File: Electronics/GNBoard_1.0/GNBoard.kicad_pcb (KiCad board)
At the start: 2 copper layers, 77.9 x 54.5 mm, 47 parts, among them K1 IR1, K10 IR4, K11 CNY_1, K12 CNY_2, K13 CNY_3, K14 CNY_4, K15 CNY_5, K16 CNY_6, K2 IR2, K3 SERVO_1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

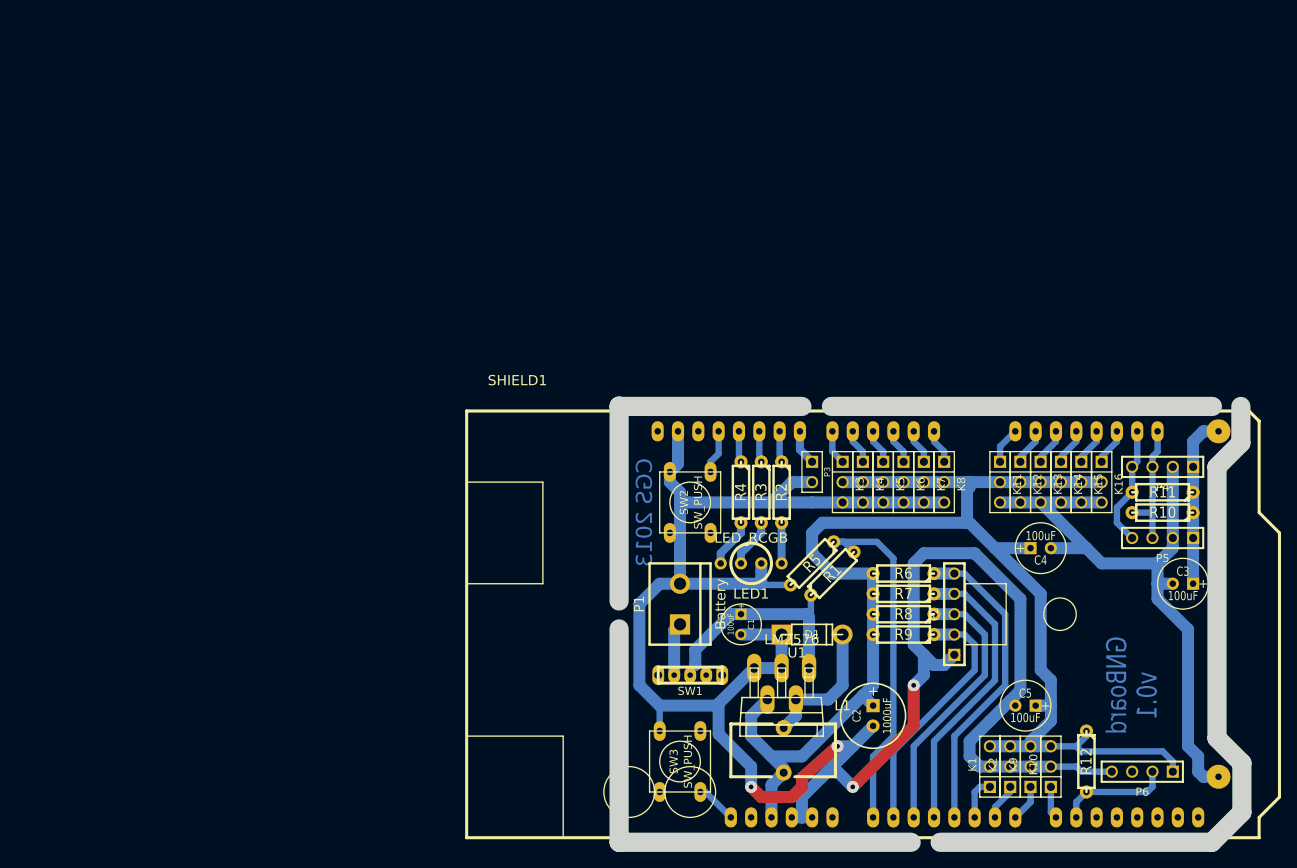
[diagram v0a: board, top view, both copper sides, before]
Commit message: Moved v0.1 to its own folder
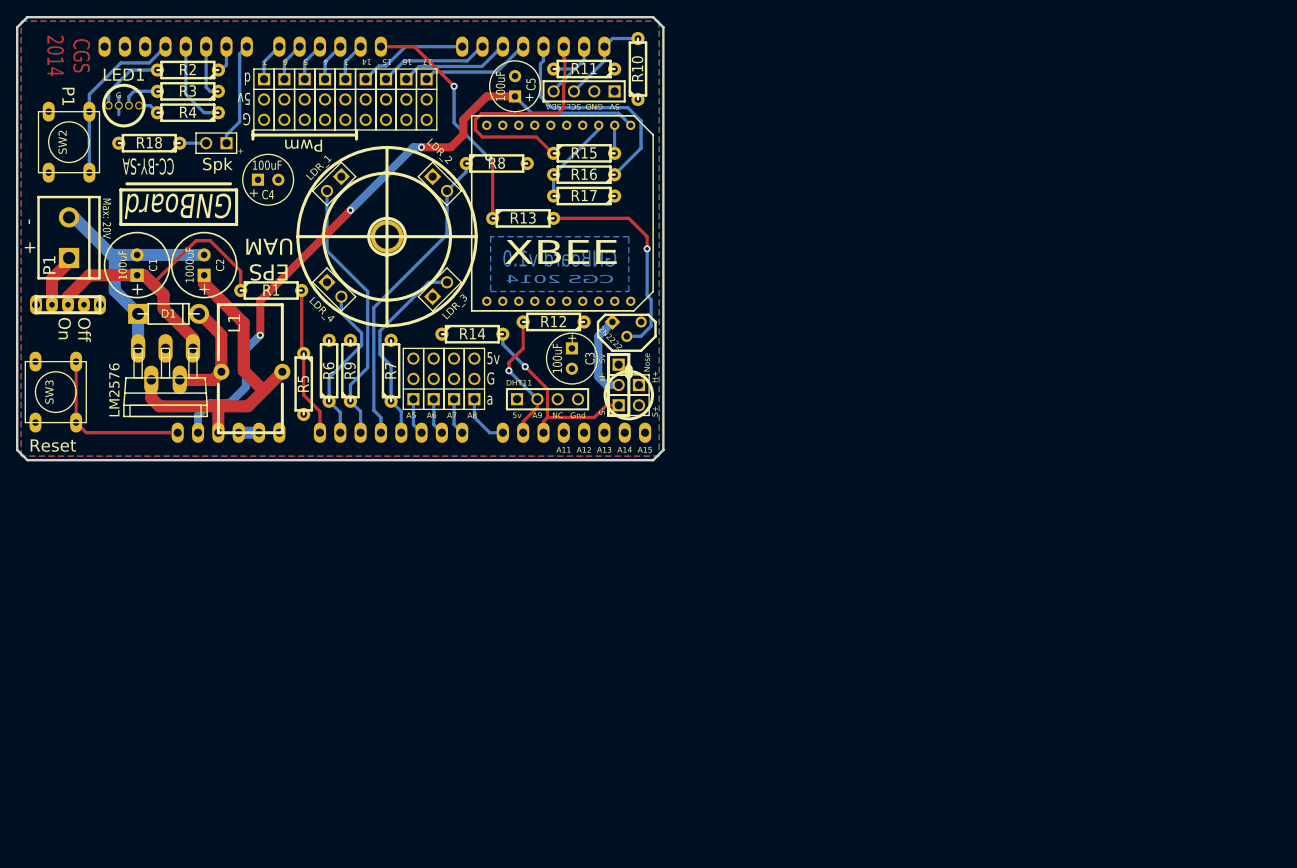
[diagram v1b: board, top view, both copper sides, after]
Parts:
- removed K15: CNY_5, PIN_ARRAY_3X1
- removed K16: CNY_6, PIN_ARRAY_3X1
- removed K8: SERVO_6, PIN_ARRAY_3X1
- added 1PIN: P***, ldr_drill, F.Cu at (96.7, 48.1)
- added M1: XBEE, xbee_r1-XBEE, F.Cu at (118.2, 45.1)
- added P10: Nose_Heater, PIN_ARRAY_2X1, F.Cu at (126.9, 66.6)
- added P11: CONN_1, PIN_ARRAY_1, F.Cu at (125.7, 64.1)
- added P7: LDR_3, PIN_ARRAY_2X1, F.Cu at (103.3, 54.7)
- added P8: LDR_4, PIN_ARRAY_2X1, F.Cu at (90.1, 54.7)
- added P9: Nose_Sense, PIN_ARRAY_2X1, F.Cu at (126.9, 69.1)
- added Q1: NPN, TO92-123, F.Cu at (126.7, 58.7)
- added R13: 10k, R3-LARGE_PADS, F.Cu at (113.7, 45.8)
- added R14: 10k, R3-LARGE_PADS, F.Cu at (107.4, 60.2)
- added R15: 4k7, R3-LARGE_PADS, F.Cu at (121.4, 37.6)
- added R16: 4k7, R3-LARGE_PADS, F.Cu at (121.4, 40.3)
- added R17: 7k5, R3-LARGE_PADS, F.Cu at (121.4, 43.0)
- added R18: 47, R3-LARGE_PADS, F.Cu at (67.0, 36.4)
- C1: footprint C1V5 -> C1V8
- L1: footprint Choke_Toroid_6,5x13mm_Vertical -> Choke_Toroid_8x16mm_Vertical
- LED1: footprint LED5_RGB_long_wide -> LED5_RGB_long
- P2: value CONN_5 -> LDR_1; footprint PIN_ARRAY_5x1 -> PIN_ARRAY_2X1
- P5: value I2C_2 -> LDR_2; footprint PIN_ARRAY_4x1 -> PIN_ARRAY_2X1
- R1: value 6k8 -> 62k
- R5: value 6k8 -> 20k
- SHIELD1: footprint ARDUINO_MEGA_SHIELD -> ARDUINO_MEGA_SHIELD_040pins_MOD
- SW1: footprint SWITCH_3Pin -> switch_power_custom
- moved C4 107.0 mm to (81.9, 40.9)
- moved C2 100.8 mm to (73.9, 51.6), turned to 90 degrees
- moved P5 100.6 mm to (103.3, 41.5), turned to 315 degrees
- moved C5 100.3 mm to (112.7, 29.3), turned to 90 degrees
- moved LED1 97.1 mm to (63.8, 31.7), turned to 0 degrees
- moved P2 94.4 mm to (90.1, 41.5), turned to 225 degrees
- moved K12 92.6 mm to (96.6, 30.9)
- moved K13 92.6 mm to (99.1, 30.9)
- moved K14 92.6 mm to (101.7, 30.9)
- moved K11 92.6 mm to (94.1, 30.9)
- moved R2 91.1 mm to (71.8, 27.2), turned to 180 degrees
- moved SW3 90.7 mm to (55.3, 67.5)
- moved SW1 90.5 mm to (56.8, 56.6)
- moved D1 89.9 mm to (69.4, 57.7)
- moved SW2 89.8 mm to (57.0, 36.2)
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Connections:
- C5 pad 1: +5V -> +3.3V
- P3 pad 2: GND -> N-0000014
- P5 pad 1: +5V -> GND
- P5 pad 2: GND -> LDR2
- P6 pad 3: N-0000082 -> (no net)
- SHIELD1 pad 13: N-0000067 -> (no net)
- SHIELD1 pad 18: CNY5 -> XB_DIN
- SHIELD1 pad 19: CNY6 -> XB_DOUT
- SHIELD1 pad 2: Servo6 -> Nose_heat
- SHIELD1 pad 3V3: N-0000040 -> +3.3V
- SHIELD1 pad AD1: LDR1 -> LDR4
- SHIELD1 pad AD10: N-0000041 -> Nose_Vout
- SHIELD1 pad AD11: N-0000039 -> (no net)
- SHIELD1 pad AD12: N-0000042 -> (no net)
- SHIELD1 pad AD13: N-0000043 -> (no net)
- SHIELD1 pad AD14: N-0000044 -> (no net)
- SHIELD1 pad AD15: N-0000045 -> (no net)
- SHIELD1 pad AD2: LDR2 -> LDR1
- SHIELD1 pad AD3: LDR3 -> LDR2
- SHIELD1 pad AD4: LDR4 -> LDR3
- SHIELD1 pad AREF: N-0000037 -> (no net)
- SHIELD1 pad V_IN: N-0000038 -> (no net)
- SW1 pad 3: N-0000046 -> (no net)
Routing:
- net GND: track 352.1 -> 36.9 mm, vias 4 -> 0
- net +5V: track 208.7 -> 41.9 mm
- net +3.3V: track 0.00 -> 80.7 mm, vias 0 -> 3
- net XB_DOUT: track 0.00 -> 31.7 mm
- net Nose_heat: track 0.00 -> 29.7 mm, vias 0 -> 2
- net XB_DIN: track 0.00 -> 28.3 mm
- net N-0000037: track 0.00 -> 27.6 mm, vias 0 -> 1
- net BattVolt: track 44.8 -> 18.7 mm
- net Nose_Vout: track 0.00 -> 24.4 mm, vias 0 -> 1
- net LDR4: track 39.0 -> 20.3 mm
- net Button1: track 5.50 -> 21.8 mm
- net ResetB: track 5.13 -> 20.8 mm
- net LDR3: track 36.5 -> 24.7 mm
- net +BATT: track 28.9 -> 40.5 mm
- net N-0000027: track 0.00 -> 11.2 mm
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- added copper zone on F.Cu, net +5V
- added copper zone on B.Cu, net GND
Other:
- board size 77.9 x 54.5 mm -> 80.8 x 55.4 mm
- net class Default: clearance 0.4 -> 0.3; trace_width 0.8 -> 0.4; via_dia 1.5 -> 0.889; via_drill 0.6 -> 0.508
- rule trace_clearance: 0.4 -> 0.3
- board text added: "+"
- board text added: "- +"
- board text added: "14"
- board text added: "15"
- board text added: "16"
- board text added: "17"
- board text added: "2N2222"
- board text added: "3"
- board text added: "4"
- board text added: "5"
- board text added: "5V"
- board text added: "5v"
- board text added: "6"
- board text added: "7"
- board text added: "A11"
- board text added: "A12"
- board text added: "A13"
- board text added: "A14"
- board text added: "A15"
- board text added: "A5"
- board text added: "A6"
- board text added: "A7"
- board text added: "A8"
- board text added: "A9"
- board text added: "CC-BY-SA"
- board text added: "CGS 2014"
- board text added: "DHT11"
- board text added: "EPS UAM"
- board text added: "G"
- board text added: "GNBoard v1.0"
- board text added: "GND"
- board text added: "Gnd"
- board text added: "H+"
- board text added: "H-"
- board text added: "Max: 20V"
- board text added: "NC"
- board text added: "Nose"
- board text added: "Off On"
- board text added: "P1"
- board text added: "Pwm"
- board text added: "Reset"
- board text added: "S+"
- board text added: "S-"
- board text added: "SCL"
- board text added: "SDA"
- board text added: "a"
- board text added: "d"
- board text removed: "CGS 2013"
- board text removed: "v0.1"

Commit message: Updated gerber files
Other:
- board text added: "http://carlosgs.es"
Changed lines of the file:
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@@
     (area 19.732134 20.474799 134.27865 76.146801)
     (thickness 1.6)
-    (drawings 83)
+    (drawings 84)
     (tracks 240)
     (zones 0)
@@
     (pcbplotparams
       (layerselection 284196865)
-      (usegerberextensions false)
+      (usegerberextensions true)
       (excludeedgelayer true)
       (linewidth 0.100000)
@@
     )
   )
+  (gr_text http://carlosgs.es (at 70.8152 44.7548) (layer B.SilkS)
+    (effects (font (size 2.032 1.524) (thickness 0.3048)) (justify mirror))
+  )
   (gr_text CC-BY-SA (at 66.9036 39.2176 180) (layer F.SilkS)
